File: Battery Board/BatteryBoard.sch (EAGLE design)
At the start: 29 parts, among them IC1 TPS63060DSCT, J0 1725656, J1 1725669, Q1 IAUC60N04S6L030HATMA1, U0 STM32L031K4U6, U1 MCP73831T-2ATI_OT, U3 STM809TWX6F

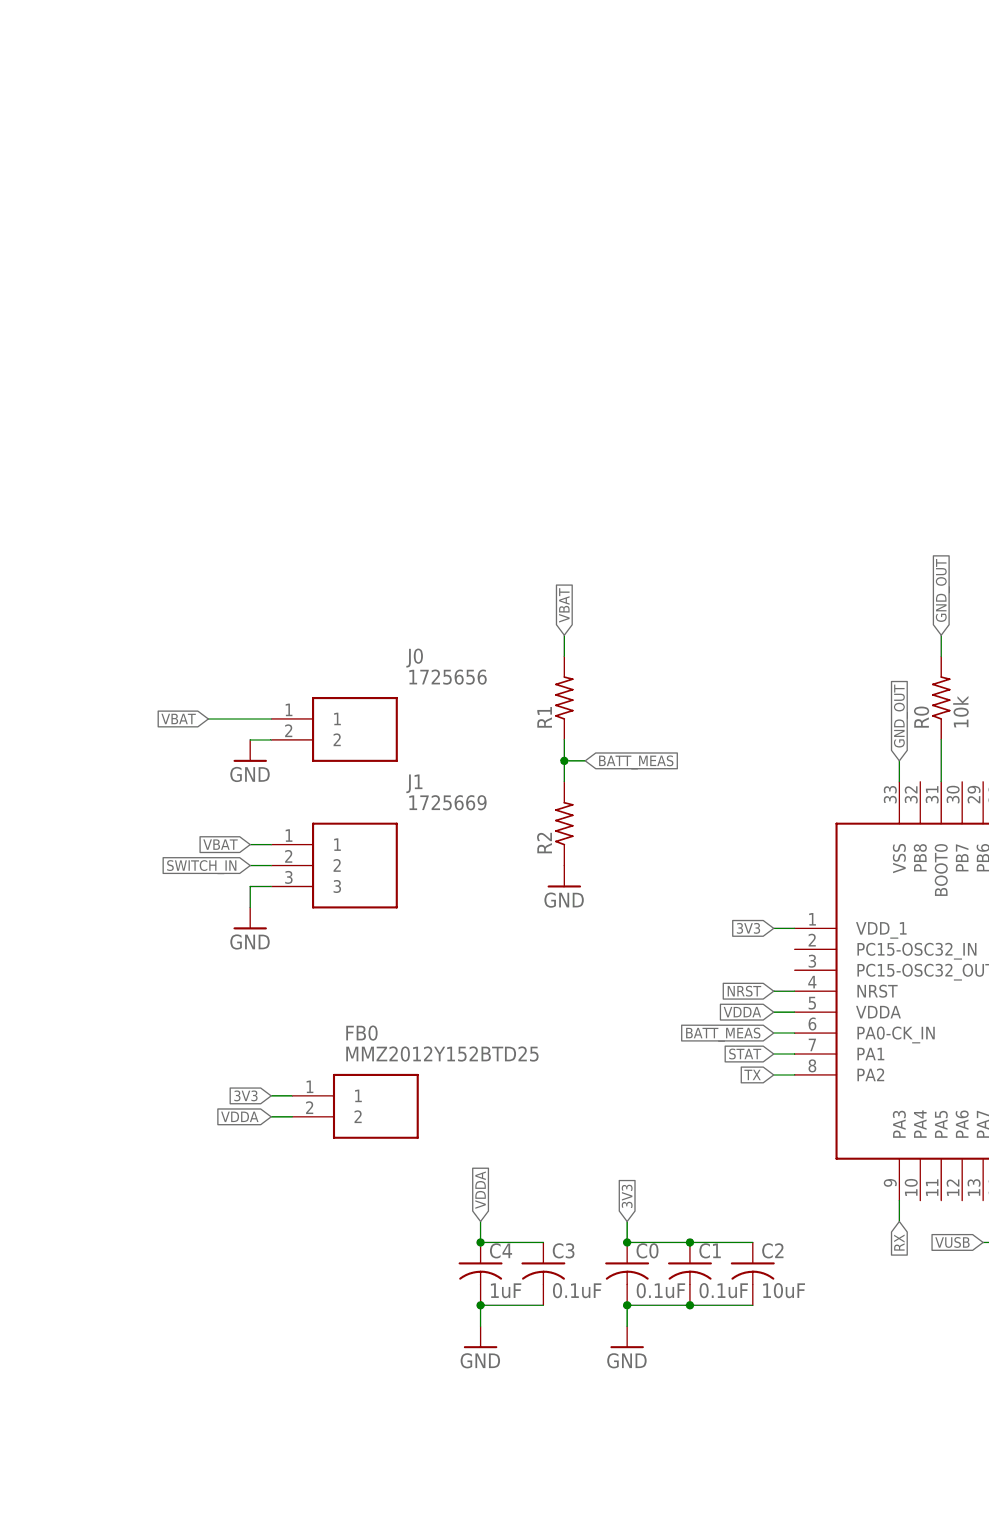
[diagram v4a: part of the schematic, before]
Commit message: Added USB and 16-pin
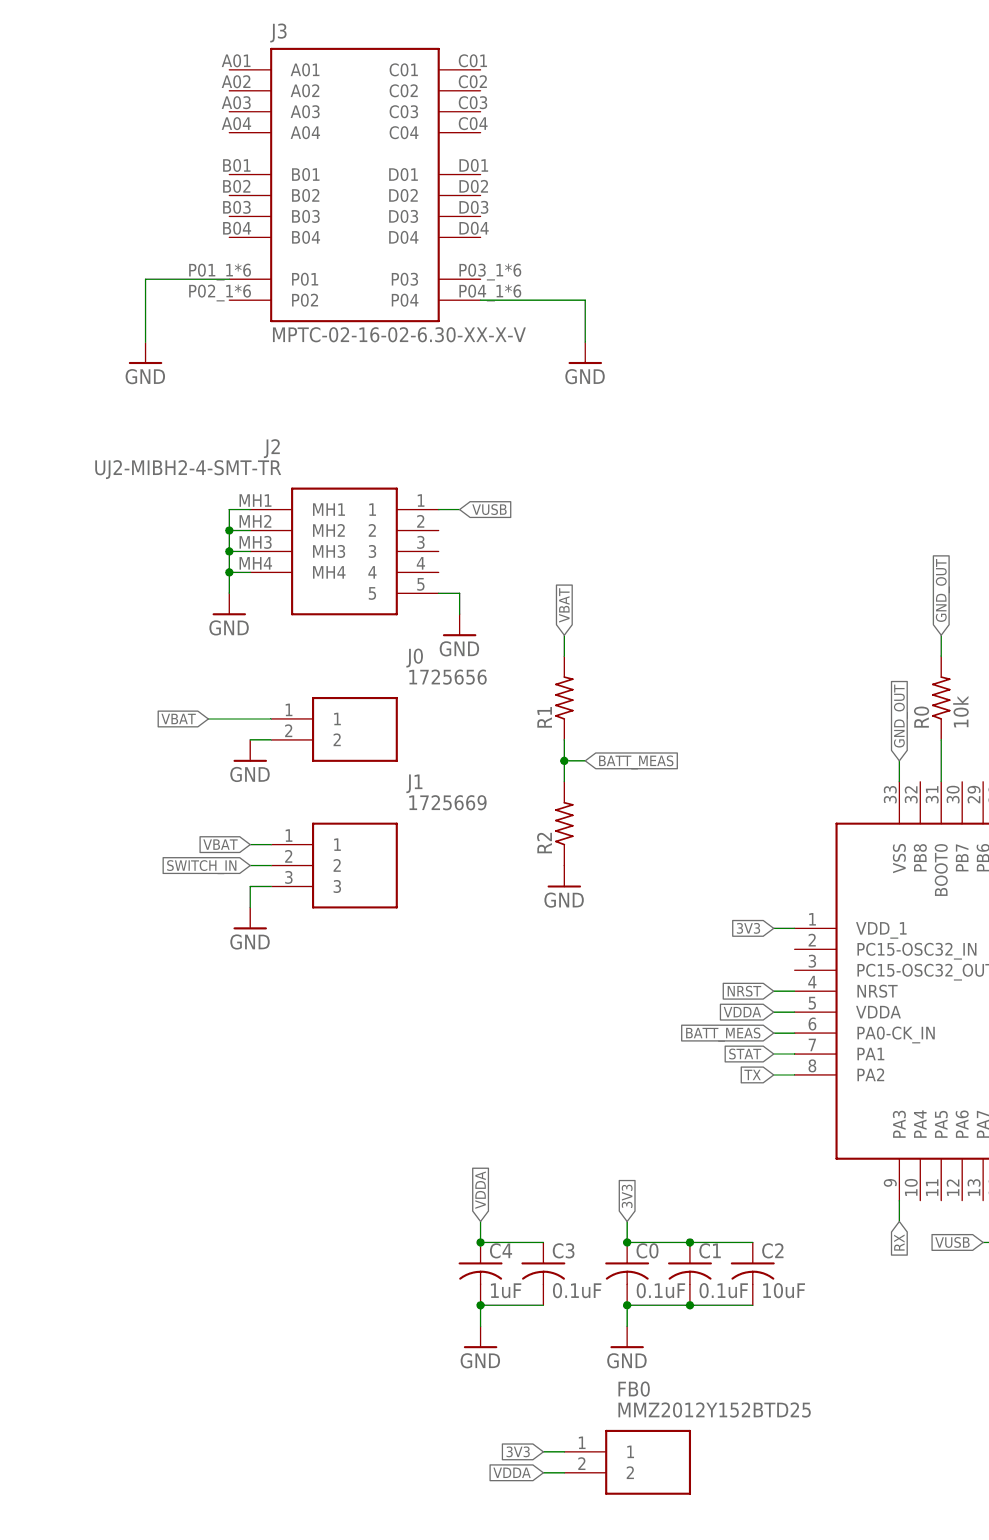
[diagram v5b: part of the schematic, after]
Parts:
- added J2: UJ2-MIBH2-4-SMT-TR, SamacSys_Parts:UJ2-MIBH2-4-SMT-TR
- added J3: MPTC-02-16-02-6.30-XX-X-V, MPTC-02-16-02-6.30-XX-X-V:MPTC-02-16-02-6.30-XX-X-V
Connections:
- net GND: now also J2.5, J2.MH1, J2.MH2, J2.MH3, J2.MH4, J3.P01, J3.P04
- net VUSB: now also J2.1
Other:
- moved on the sheet: FB0
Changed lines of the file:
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@@
 <part name="J1" library="SamacSys_Parts" deviceset="1725669" device=""/>
 <part name="GND1" library="supply1" library_urn="urn:adsk.eagle:library:371" deviceset="GND" device=""/>
+<part name="J2" library="SamacSys_Parts" deviceset="UJ2-MIBH2-4-SMT-TR" device=""/>
+<part name="GND4" library="supply1" library_urn="urn:adsk.eagle:library:371" deviceset="GND" device=""/>
+<part name="GND13" library="supply1" library_urn="urn:adsk.eagle:library:371" deviceset="GND" device=""/>
+<part name="J3" library="MPTC-02-16-02-6.30-XX-X-V" deviceset="MPTC-02-16-02-6.30-XX-X-V" device=""/>
+<part name="GND14" library="supply1" library_urn="urn:adsk.eagle:library:371" deviceset="GND" device=""/>
+<part name="GND15" library="supply1" library_urn="urn:adsk.eagle:library:371" deviceset="GND" device=""/>
 </parts>
 <sheets>
@@
 <attribute name="VALUE" x="-25.4" y="-2.54" size="1.778" layer="96"/>
 </instance>
-<instance part="FB0" gate="G$1" x="-45.72" y="30.48" smashed="yes">
-<attribute name="NAME" x="-39.37" y="38.1" size="1.778" layer="95" align="center-left"/>
-<attribute name="VALUE" x="-39.37" y="35.56" size="1.778" layer="96" align="center-left"/>
+<instance part="FB0" gate="G$1" x="-12.7" y="-12.7" smashed="yes">
+<attribute name="NAME" x="-6.35" y="-5.08" size="1.778" layer="95" align="center-left"/>
+<attribute name="VALUE" x="-6.35" y="-7.62" size="1.778" layer="96" align="center-left"/>
 </instance>
 <instance part="R1" gate="G$1" x="-12.7" y="78.74" smashed="yes" rot="R90">
@@
 <instance part="GND1" gate="1" x="-50.8" y="50.8" smashed="yes">
 <attribute name="VALUE" x="-53.34" y="48.26" size="1.778" layer="96"/>
+</instance>
+<instance part="J2" gate="G$1" x="-27.94" y="101.6" smashed="yes" rot="MR0">
+<attribute name="NAME" x="-46.99" y="109.22" size="1.778" layer="95" rot="MR0" align="center-left"/>
+<attribute name="VALUE" x="-46.99" y="106.68" size="1.778" layer="96" rot="MR0" align="center-left"/>
+</instance>
+<instance part="GND4" gate="1" x="-25.4" y="86.36" smashed="yes">
+<attribute name="VALUE" x="-27.94" y="83.82" size="1.778" layer="96"/>
+</instance>
+<instance part="GND13" gate="1" x="-53.34" y="88.9" smashed="yes">
+<attribute name="VALUE" x="-55.88" y="86.36" size="1.778" layer="96"/>
+</instance>
+<instance part="J3" gate="G$1" x="-38.1" y="142.24" smashed="yes">
+<attribute name="NAME" x="-48.26" y="158.75" size="1.778" layer="95"/>
+<attribute name="VALUE" x="-48.26" y="121.92" size="1.778" layer="96"/>
+</instance>
+<instance part="GND14" gate="1" x="-63.5" y="119.38" smashed="yes">
+<attribute name="VALUE" x="-66.04" y="116.84" size="1.778" layer="96"/>
+</instance>
+<instance part="GND15" gate="1" x="-10.16" y="119.38" smashed="yes">
+<attribute name="VALUE" x="-12.7" y="116.84" size="1.778" layer="96"/>
 </instance>
 </instances>
@@
 <pinref part="GND1" gate="1" pin="GND"/>
 </segment>
+<segment>
+<pinref part="J2" gate="G$1" pin="5"/>
+<wire x1="-27.94" y1="91.44" x2="-25.4" y2="91.44" width="0.1524" layer="91"/>
+<wire x1="-25.4" y1="91.44" x2="-25.4" y2="88.9" width="0.1524" layer="91"/>
+<pinref part="GND4" gate="1" pin="GND"/>
+</segment>
+<segment>
+<pinref part="J2" gate="G$1" pin="MH1"/>
+<wire x1="-50.8" y1="101.6" x2="-53.34" y2="101.6" width="0.1524" layer="91"/>
+<wire x1="-53.34" y1="101.6" x2="-53.34" y2="99.06" width="0.1524" layer="91"/>
+<pinref part="J2" gate="G$1" pin="MH4"/>
+<wire x1="-53.34" y1="99.06" x2="-53.34" y2="96.52" width="0.1524" layer="91"/>
+<wire x1="-53.34" y1="93.98" x2="-53.34" y2="91.44" width="0.1524" layer="91"/>
+<wire x1="-50.8" y1="93.98" x2="-53.34" y2="93.98" width="0.1524" layer="91"/>
+<junction x="-53.34" y="93.98"/>
+<wire x1="-53.34" y1="93.98" x2="-53.34" y2="96.52" width="0.1524" layer="91"/>
+<pinref part="J2" gate="G$1" pin="MH2"/>
+<wire x1="-50.8" y1="99.06" x2="-53.34" y2="99.06" width="0.1524" layer="91"/>
+<junction x="-53.34" y="99.06"/>
+<pinref part="J2" gate="G$1" pin="MH3"/>
+<wire x1="-50.8" y1="96.52" x2="-53.34" y2="96.52" width="0.1524" layer="91"/>
+<junction x="-53.34" y="96.52"/>
+<pinref part="GND13" gate="1" pin="GND"/>
+</segment>
+<segment>
+<pinref part="J3" gate="G$1" pin="P01"/>
+<wire x1="-53.34" y1="129.54" x2="-63.5" y2="129.54" width="0.1524" layer="91"/>
+<wire x1="-63.5" y1="129.54" x2="-63.5" y2="121.92" width="0.1524" layer="91"/>
+<pinref part="GND14" gate="1" pin="GND"/>
+</segment>
+<segment>
+<pinref part="J3" gate="G$1" pin="P04"/>
+<wire x1="-22.86" y1="127" x2="-10.16" y2="127" width="0.1524" layer="91"/>
+<wire x1="-10.16" y1="127" x2="-10.16" y2="121.92" width="0.1524" layer="91"/>
+<pinref part="GND15" gate="1" pin="GND"/>
+</segment>
 </net>
 <net name="VDDA" class="0">
@@
 <segment>
 <pinref part="FB0" gate="G$1" pin="2"/>
-<wire x1="-45.72" y1="27.94" x2="-48.26" y2="27.94" width="0.1524" layer="91"/>
-<label x="-48.26" y="27.94" size="1.27" layer="95" rot="R180" xref="yes"/>
+<wire x1="-12.7" y1="-15.24" x2="-15.24" y2="-15.24" width="0.1524" layer="91"/>
+<label x="-15.24" y="-15.24" size="1.27" layer="95" rot="R180" xref="yes"/>
 </segment>
 </net>
@@
 <pinref part="LED1" gate="G$1" pin="A"/>
 </segment>
+<segment>
+<pinref part="J2" gate="G$1" pin="1"/>
+<wire x1="-27.94" y1="101.6" x2="-25.4" y2="101.6" width="0.1524" layer="91"/>
+<label x="-25.4" y="101.6" size="1.27" layer="95" xref="yes"/>
+</segment>
 </net>
 <net name="LED1" class="0">
@@
 <segment>
 <pinref part="FB0" gate="G$1" pin="1"/>
-<wire x1="-45.72" y1="30.48" x2="-48.26" y2="30.48" width="0.1524" layer="91"/>
-<label x="-48.26" y="30.48" size="1.27" layer="95" rot="R180" xref="yes"/>
-</segment>
-<segment>
+<wire x1="-12.7" y1="-12.7" x2="-15.24" y2="-12.7" width="0.1524" layer="91"/>
+<label x="-15.24" y="-12.7" size="1.27" layer="95" rot="R180" xref="yes"/>
+</segment>
+<segment>

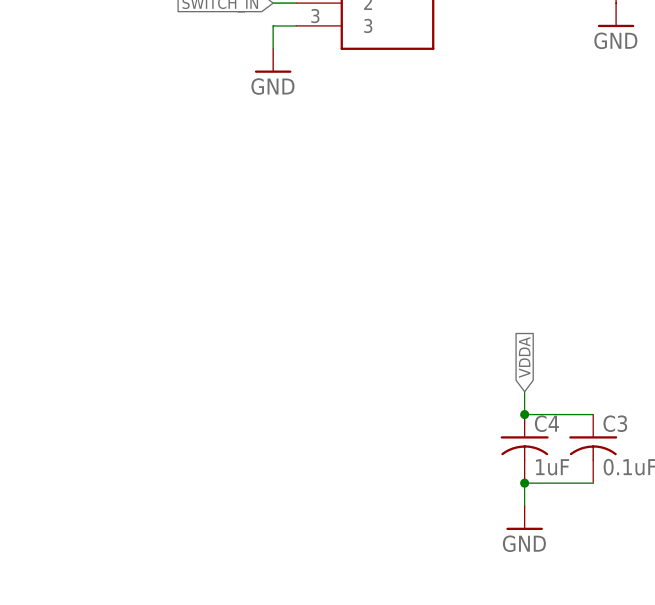
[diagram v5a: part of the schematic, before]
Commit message: Added JSTPH2
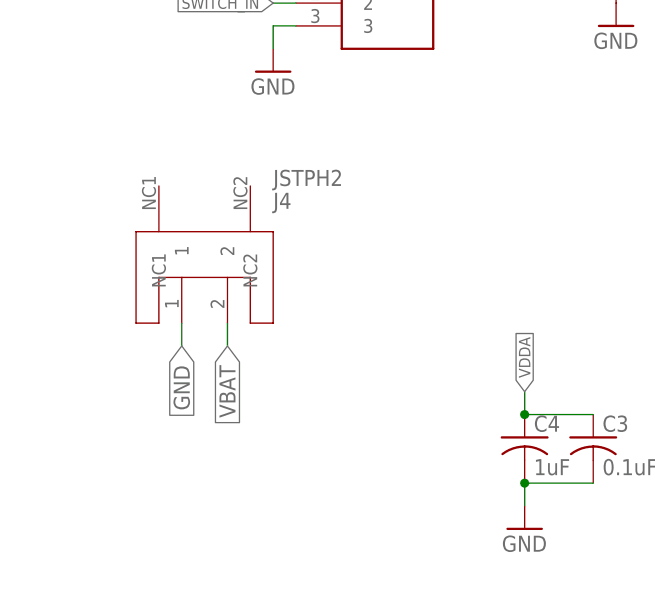
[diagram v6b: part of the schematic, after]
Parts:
- added J4: JSTPH2, Connect:JSTPH2
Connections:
- net GND: now also J4.1
- net VBAT: now also J4.2
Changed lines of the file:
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@@
 <part name="GND14" library="supply1" library_urn="urn:adsk.eagle:library:371" deviceset="GND" device=""/>
 <part name="GND15" library="supply1" library_urn="urn:adsk.eagle:library:371" deviceset="GND" device=""/>
+<part name="J4" library="Connect" deviceset="JSTPH2" device="" package3d_urn="urn:adsk.eagle:package:15955189/2"/>
 </parts>
 <sheets>
@@
 <instance part="GND15" gate="1" x="-10.16" y="119.38" smashed="yes">
 <attribute name="VALUE" x="-12.7" y="116.84" size="1.778" layer="96"/>
+</instance>
+<instance part="J4" gate="G$1" x="-58.42" y="27.94" smashed="yes">
+<attribute name="NAME" x="-50.8" y="35.56" size="1.778" layer="95"/>
+<attribute name="VALUE" x="-50.8" y="38.1" size="1.778" layer="96"/>
 </instance>
 </instances>
@@
 <pinref part="GND15" gate="1" pin="GND"/>
 </segment>
+<segment>
+<pinref part="J4" gate="G$1" pin="1"/>
+<wire x1="-60.96" y1="22.86" x2="-60.96" y2="20.32" width="0.1524" layer="91"/>
+<label x="-60.96" y="20.32" size="1.778" layer="95" rot="R270" xref="yes"/>
+</segment>
 </net>
 <net name="VDDA" class="0">
@@
 <label x="-50.8" y="60.96" size="1.27" layer="95" rot="R180" xref="yes"/>
 </segment>
+<segment>
+<pinref part="J4" gate="G$1" pin="2"/>
+<wire x1="-55.88" y1="22.86" x2="-55.88" y2="20.32" width="0.1524" layer="91"/>
+<label x="-55.88" y="20.32" size="1.778" layer="95" rot="R270" xref="yes"/>
+</segment>
 </net>

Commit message: Further development
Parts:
- added J5: MPTC-02-04-02-6.30-XX-X-V-LC, MPTC-02-04-02-6.30-XX-X-V-LC:MPTC-02-04-02-6.30-XX-X-V-LC
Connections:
- net GND: now also J5.P01, J5.P04
- net VBAT: now also J5.P03
- net VUSB: now also J5.P02
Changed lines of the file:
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@@
 <part name="GND15" library="supply1" library_urn="urn:adsk.eagle:library:371" deviceset="GND" device=""/>
 <part name="J4" library="Connect" deviceset="JSTPH2" device="" package3d_urn="urn:adsk.eagle:package:15955189/2"/>
+<part name="J5" library="MPTC-02-04-02-6.30-XX-X-V-LC" deviceset="MPTC-02-04-02-6.30-XX-X-V-LC" device=""/>
+<part name="GND24" library="supply1" library_urn="urn:adsk.eagle:library:371" deviceset="GND" device=""/>
+<part name="GND25" library="supply1" library_urn="urn:adsk.eagle:library:371" deviceset="GND" device=""/>
 </parts>
 <sheets>
@@
 <attribute name="VALUE" x="-66.04" y="116.84" size="1.778" layer="96"/>
 </instance>
-<instance part="GND15" gate="1" x="-10.16" y="119.38" smashed="yes">
-<attribute name="VALUE" x="-12.7" y="116.84" size="1.778" layer="96"/>
+<instance part="GND15" gate="1" x="-12.7" y="119.38" smashed="yes">
+<attribute name="VALUE" x="-15.24" y="116.84" size="1.778" layer="96"/>
 </instance>
 <instance part="J4" gate="G$1" x="-58.42" y="27.94" smashed="yes">
 <attribute name="NAME" x="-50.8" y="35.56" size="1.778" layer="95"/>
 <attribute name="VALUE" x="-50.8" y="38.1" size="1.778" layer="96"/>
+</instance>
+<instance part="J5" gate="G$1" x="-38.1" y="175.26" smashed="yes">
+<attribute name="NAME" x="-48.26" y="184.15" size="1.778" layer="95"/>
+<attribute name="VALUE" x="-48.26" y="162.56" size="1.778" layer="96"/>
+</instance>
+<instance part="GND24" gate="1" x="-66.04" y="160.02" smashed="yes">
+<attribute name="VALUE" x="-68.58" y="157.48" size="1.778" layer="96"/>
+</instance>
+<instance part="GND25" gate="1" x="-10.16" y="160.02" smashed="yes">
+<attribute name="VALUE" x="-12.7" y="157.48" size="1.778" layer="96"/>
 </instance>
 </instances>
@@
 <segment>
 <pinref part="J3" gate="G$1" pin="P04"/>
-<wire x1="-22.86" y1="127" x2="-10.16" y2="127" width="0.1524" layer="91"/>
-<wire x1="-10.16" y1="127" x2="-10.16" y2="121.92" width="0.1524" layer="91"/>
+<wire x1="-22.86" y1="127" x2="-12.7" y2="127" width="0.1524" layer="91"/>
+<wire x1="-12.7" y1="127" x2="-12.7" y2="121.92" width="0.1524" layer="91"/>
 <pinref part="GND15" gate="1" pin="GND"/>
 </segment>
@@
 <wire x1="-60.96" y1="22.86" x2="-60.96" y2="20.32" width="0.1524" layer="91"/>
 <label x="-60.96" y="20.32" size="1.778" layer="95" rot="R270" xref="yes"/>
+</segment>
+<segment>
+<pinref part="J5" gate="G$1" pin="P01"/>
+<wire x1="-53.34" y1="170.18" x2="-66.04" y2="170.18" width="0.1524" layer="91"/>
+<wire x1="-66.04" y1="170.18" x2="-66.04" y2="162.56" width="0.1524" layer="91"/>
+<pinref part="GND24" gate="1" pin="GND"/>
+</segment>
+<segment>
+<pinref part="J5" gate="G$1" pin="P04"/>
+<wire x1="-22.86" y1="167.64" x2="-10.16" y2="167.64" width="0.1524" layer="91"/>
+<wire x1="-10.16" y1="167.64" x2="-10.16" y2="162.56" width="0.1524" layer="91"/>
+<pinref part="GND25" gate="1" pin="GND"/>
 </segment>
 </net>
@@
 <label x="-55.88" y="20.32" size="1.778" layer="95" rot="R270" xref="yes"/>
 </segment>
+<segment>
+<pinref part="J5" gate="G$1" pin="P03"/>
+<wire x1="-22.86" y1="170.18" x2="-17.78" y2="170.18" width="0.1524" layer="91"/>
+<label x="-17.78" y="170.18" size="1.27" layer="95" xref="yes"/>
+</segment>
 </net>
 <net name="I2C_SDA" class="0">
@@
 <label x="-25.4" y="101.6" size="1.27" layer="95" xref="yes"/>
 </segment>
-</net>
+<segment>
+<pinref part="J5" gate="G$1" pin="P02"/>
+<wire x1="-53.34" y1="167.64" x2="-58.42" y2="167.64" width="0.1524" layer="91"/>
+<label x="-58.42" y="167.64" size="1.27" layer="95" rot="R180" xref="yes"/>
+</segment>
+</net>
